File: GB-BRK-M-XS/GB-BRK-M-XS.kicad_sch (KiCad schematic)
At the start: 4 parts, among them J1 CONN_02X16, J2 Conn_GameBoy_Cartridge

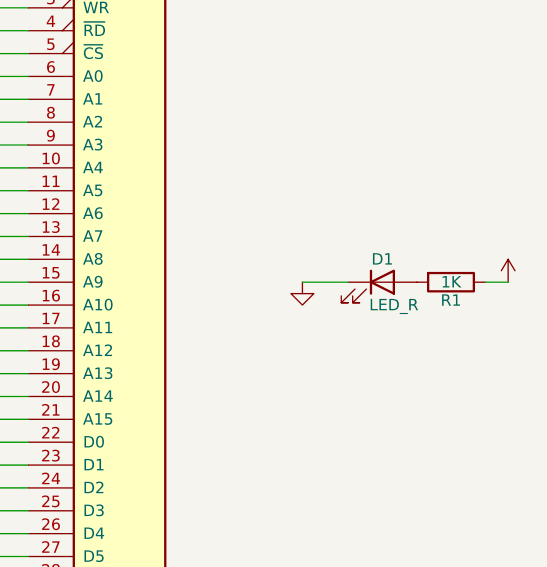
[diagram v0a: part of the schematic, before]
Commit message: Upgrade projects to KiCad 7
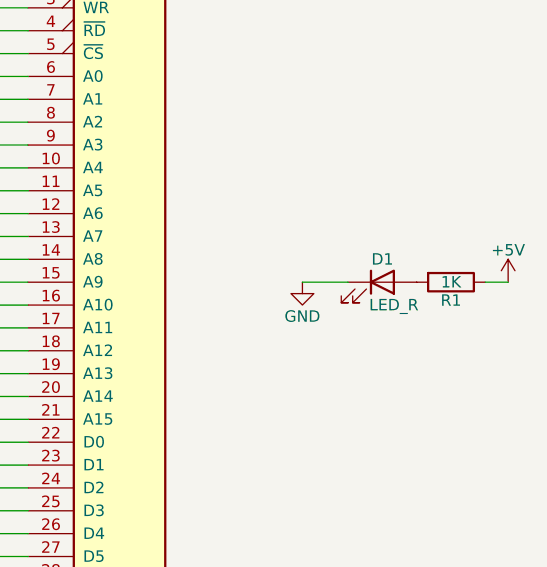
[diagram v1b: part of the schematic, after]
